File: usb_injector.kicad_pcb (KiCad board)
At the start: 2 copper layers, 43 x 23 mm, 10 parts, among them J1 USB_MALE, J2 USB_FEMALE, J3 USB_FEMALE_WITH_ID, J4 USB_FEMALE_WITH_ID, J5 USB_MALE, J6 USB_FEMALE, J7 USB_FEMALE_WITH_ID, J8 USB_FEMALE_WITH_ID, P1 CONN_6, P2 CONN_6

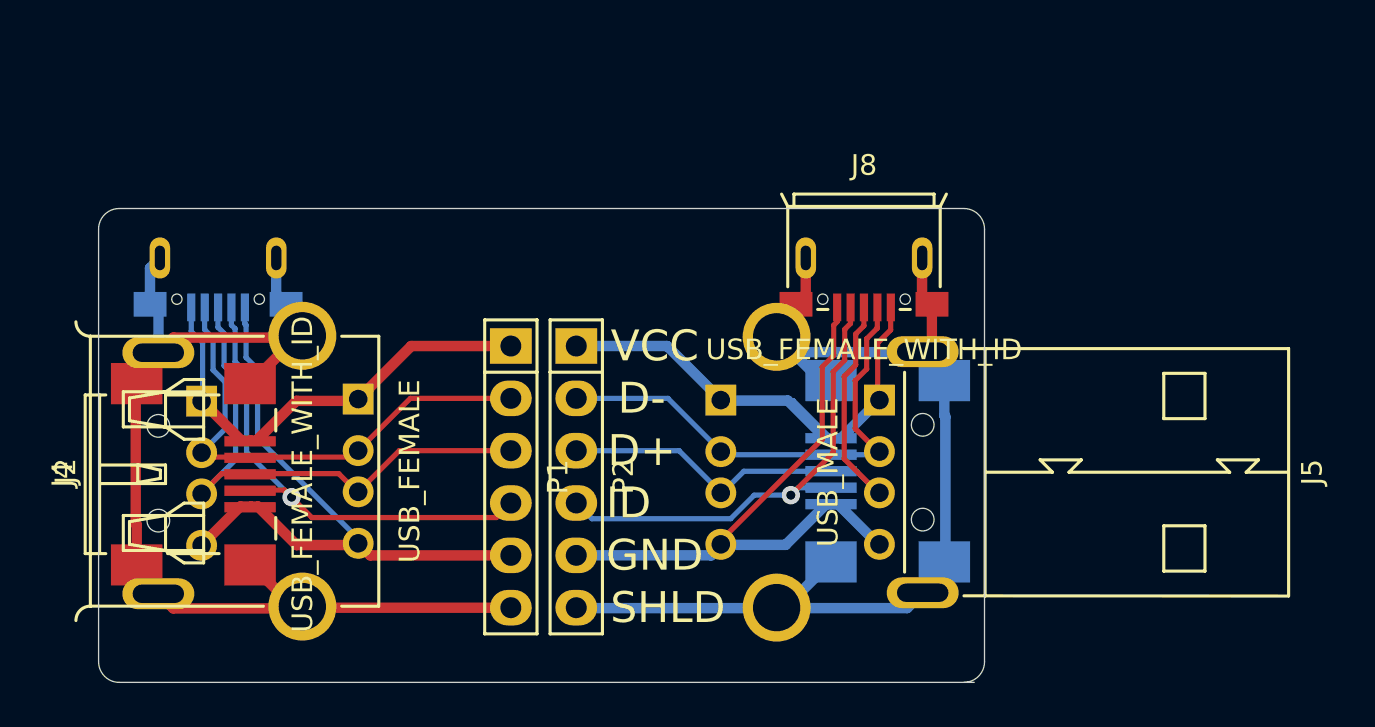
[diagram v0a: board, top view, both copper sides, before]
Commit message: updated components, fixed .1" headers spacing, rearranged header pinout such that full size USB-connectors have length-matched traces and moved USB-mini connector alongside USB-micro connector
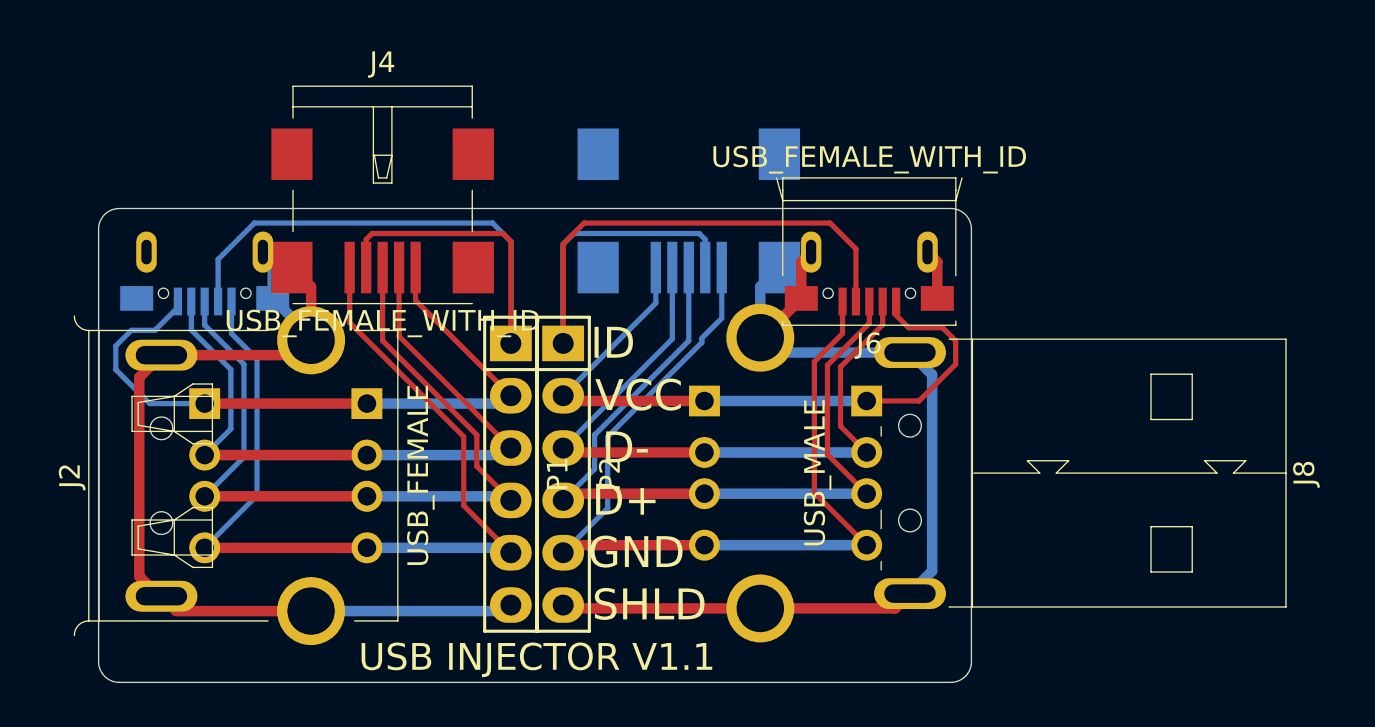
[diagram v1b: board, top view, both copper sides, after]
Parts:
- J5: value USB_MALE -> USB_FEMALE_WITH_ID; footprint Connectors:USB_A_Male -> Connectors:USB_Mini-B_Female; moved to B.Cu
- J6: value USB_FEMALE -> USB_FEMALE_WITH_ID; footprint Connectors:USB_A_Female -> Connectors:USB_Micro-B_Female_Wellco_AUSB_1011_05S2; moved to F.Cu
- J7: value USB_FEMALE_WITH_ID -> USB_FEMALE; footprint Connectors:USB_Mini-B_Female -> Connectors:USB_A_Female
- J8: value USB_FEMALE_WITH_ID -> USB_MALE; footprint Connectors:USB_Micro-B_Female_Wellco_AUSB_1011_05S2 -> Connectors:USB_A_Male
- moved J5 11.3 mm to (88.6, 62.9), turned to 0 degrees
- moved J4 10.6 mm to (73.8, 62.9), turned to 180 degrees
- moved J6 8.65 mm to (97.4, 64.5), turned to 180 degrees
- moved J7 6.40 mm to (89.4, 69.3)
- moved J8 4.69 mm to (97.3, 69.3), turned to 270 degrees
- moved J3 0.71 mm to (65.2, 64.5)
- moved P2 0.65 mm to (82.5, 72.9)
- moved J2 0.48 mm to (73.0, 69.5)
- moved J1 0.19 mm to (65.2, 69.5)
- moved P1 0.13 mm to (80.0, 72.9)
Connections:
- J7 pad 4: Net-(J7-Pad4) -> Net-(J5-Pad5)
- J7 pad 5: Net-(J5-Pad4) -> Net-(J5-Pad6)
- J8 pad 4: Net-(J7-Pad4) -> Net-(J5-Pad5)
- J8 pad 5: Net-(J5-Pad4) -> Net-(J5-Pad6)
- P1 pad 1: Net-(J1-Pad1) -> Net-(J3-Pad4)
- P1 pad 2: Net-(J1-Pad2) -> Net-(J1-Pad1)
- P1 pad 3: Net-(J1-Pad3) -> Net-(J1-Pad2)
- P1 pad 4: Net-(J3-Pad4) -> Net-(J1-Pad3)
- P2 pad 1: Net-(J5-Pad1) -> Net-(J5-Pad4)
- P2 pad 2: Net-(J5-Pad2) -> Net-(J5-Pad1)
- P2 pad 3: Net-(J5-Pad3) -> Net-(J5-Pad2)
- P2 pad 4: Net-(J7-Pad4) -> Net-(J5-Pad3)
- P2 pad 5: Net-(J5-Pad4) -> Net-(J5-Pad5)
- P2 pad 6: Net-(J5-Pad5) -> Net-(J5-Pad6)
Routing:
- net Net-(J5-Pad6): track 0.00 -> 48.8 mm
- net Net-(J7-Pad4): track 23.6 -> 0.00 mm, vias 1 -> 0
- net Net-(J1-Pad4): track 30.6 -> 45.9 mm
- net Net-(J1-Pad3): track 26.7 -> 40.1 mm
- net Net-(J5-Pad3): track 26.5 -> 39.7 mm
- net Net-(J1-Pad1): track 22.5 -> 33.9 mm
- net Net-(J3-Pad4): track 24.6 -> 35.9 mm, vias 1 -> 0
- net Net-(J1-Pad2): track 24.2 -> 35.3 mm
- net Net-(J5-Pad2): track 23.8 -> 34.5 mm
- net Net-(J5-Pad5): track 53.4 -> 45.4 mm
- net Net-(J1-Pad5): track 55.1 -> 48.5 mm
- net Net-(J5-Pad4): track 30.4 -> 35.9 mm
- net Net-(J5-Pad1): track 28.2 -> 33.2 mm
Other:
- board size 43 x 23 mm -> 42.4 x 23 mm
- board text added: "USB INJECTOR V1.1"
- board text removed: "USB INJECTOR V1.0"
